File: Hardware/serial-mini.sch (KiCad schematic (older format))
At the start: 13 parts, among them J1 PICKIT V3 Header, U3 DSPIC33CK64MP102

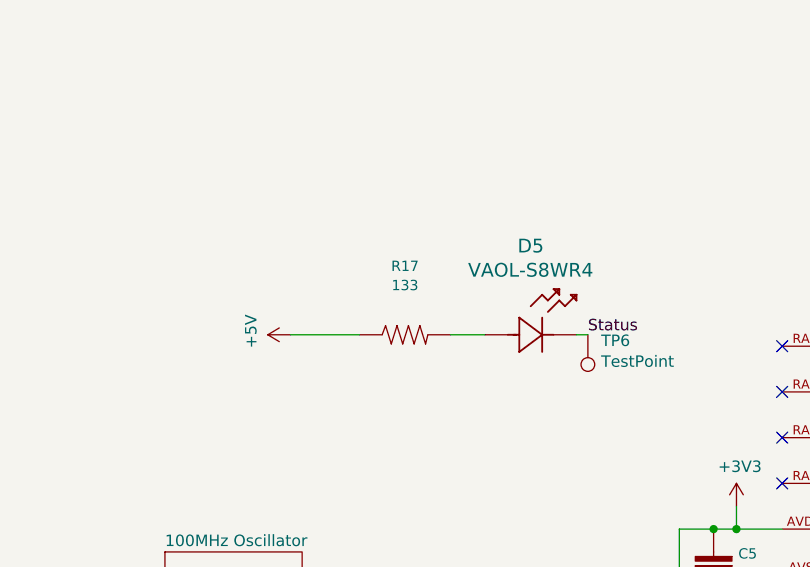
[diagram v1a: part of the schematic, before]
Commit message: Fix faulty debounce circuit
Used wrong value resistor/misplaced on each switch.
Also adjusted value of RC circuits for a time constant of 1 microsecond (was 1 millisecond before)
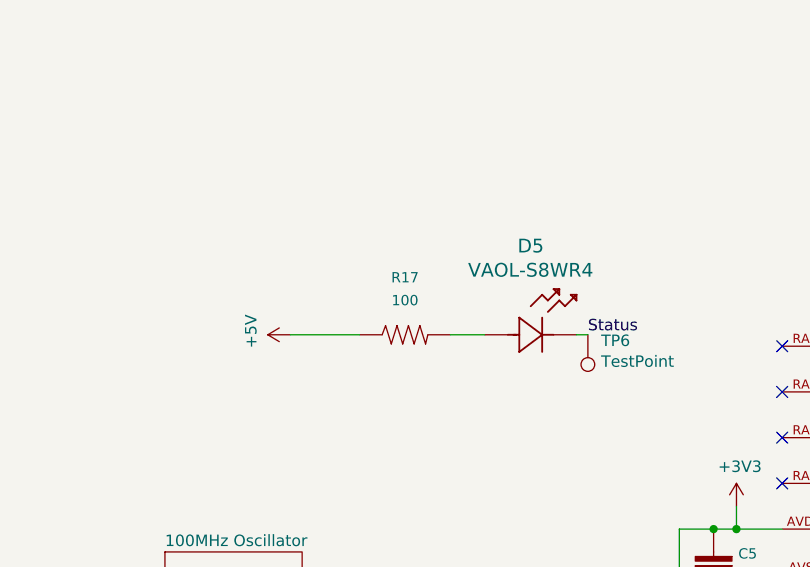
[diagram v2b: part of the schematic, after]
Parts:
- R17: value 133 -> 100
- TP6: footprint TestPoint:TestPoint_THTPad_1.0x1.0mm_Drill0.5mm -> TestPoint:TestPoint_Pad_1.0x1.0mm
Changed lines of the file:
@@
 U 1 1 5F3D4344
 P 5450 4800
-F 0 "R17" H 5450 5100 45  0000 C CNN
-F 1 "133" H 5450 5016 45  0000 C CNN
+F 0 "R17" H 5450 5050 45  0000 C CNN
+F 1 "100" H 5450 4950 45  0000 C CNN
 F 2 "Resistor_SMD:R_0603_1608Metric_Pad1.05x0.95mm_HandSolder" H 5450 4950 20  0001 C CNN
 F 3 "" H 5450 4800 60  0001 C CNN
@@
 F 0 "TP6" H 6192 4826 50  0000 R CNN
 F 1 "TestPoint" H 6192 4917 50  0000 R CNN
-F 2 "TestPoint:TestPoint_THTPad_1.0x1.0mm_Drill0.5mm" H 6450 4800 50  0001 C CNN
+F 2 "TestPoint:TestPoint_Pad_1.0x1.0mm" H 6450 4800 50  0001 C CNN
 F 3 "~" H 6450 4800 50  0001 C CNN
 	1    6250 4800

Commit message: Add BOM
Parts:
- J1: value PICKIT V3 Header -> 801-47-006-10-012000
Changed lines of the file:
@@
 P 10850 4250
 F 0 "J1" V 10765 4828 45  0000 L CNN
-F 1 "PICKIT V3 Header" V 10849 4828 45  0000 L CNN
+F 1 "801-47-006-10-012000" V 10849 4828 45  0000 L CNN
 F 2 "footprints:PICKITv3" H 10850 4950 20  0001 C CNN
 F 3 "" H 10850 4250 50  0001 C CNN
